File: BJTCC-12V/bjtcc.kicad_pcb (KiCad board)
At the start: 2 copper layers, 9 parts, among them J1 Screw_Terminal_1x04, P1 CONN_02X01, Q1 ASZ15, Q2 ASZ15

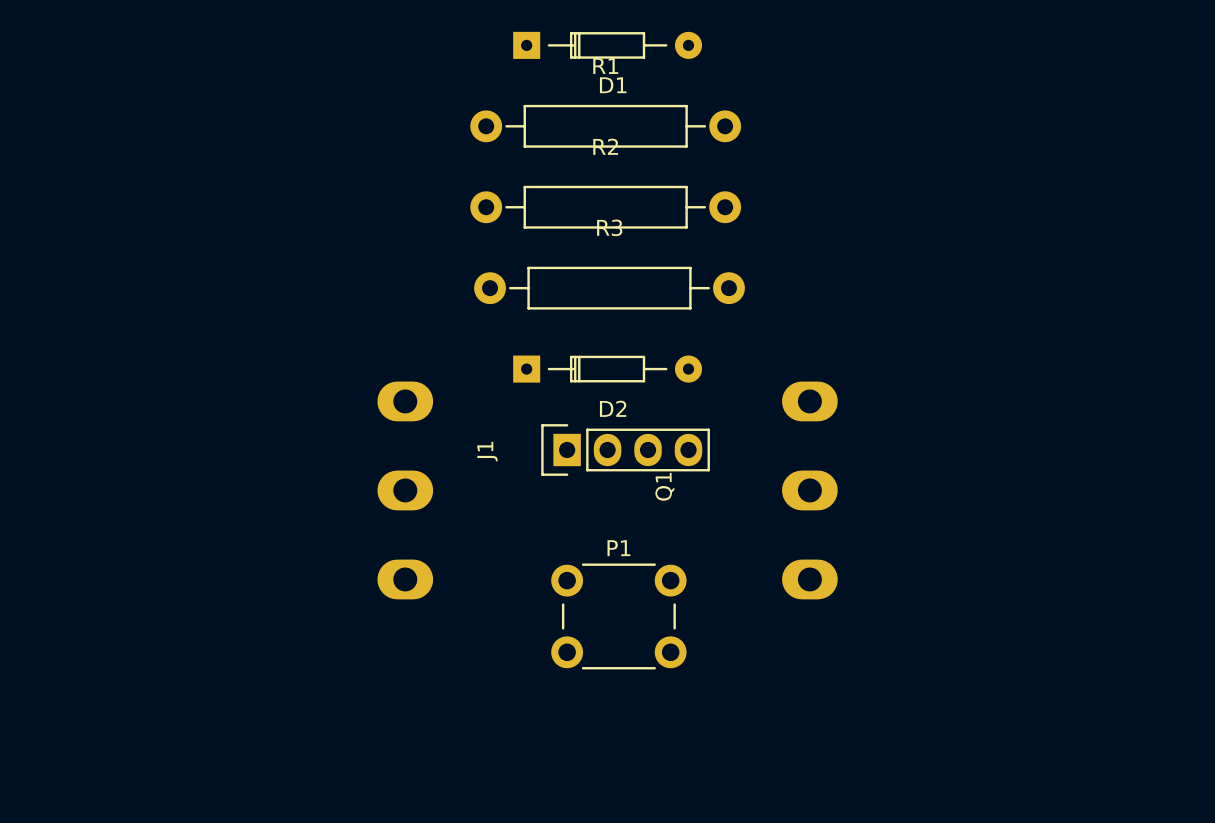
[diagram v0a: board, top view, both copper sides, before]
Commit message: rough placing footprints on PCB
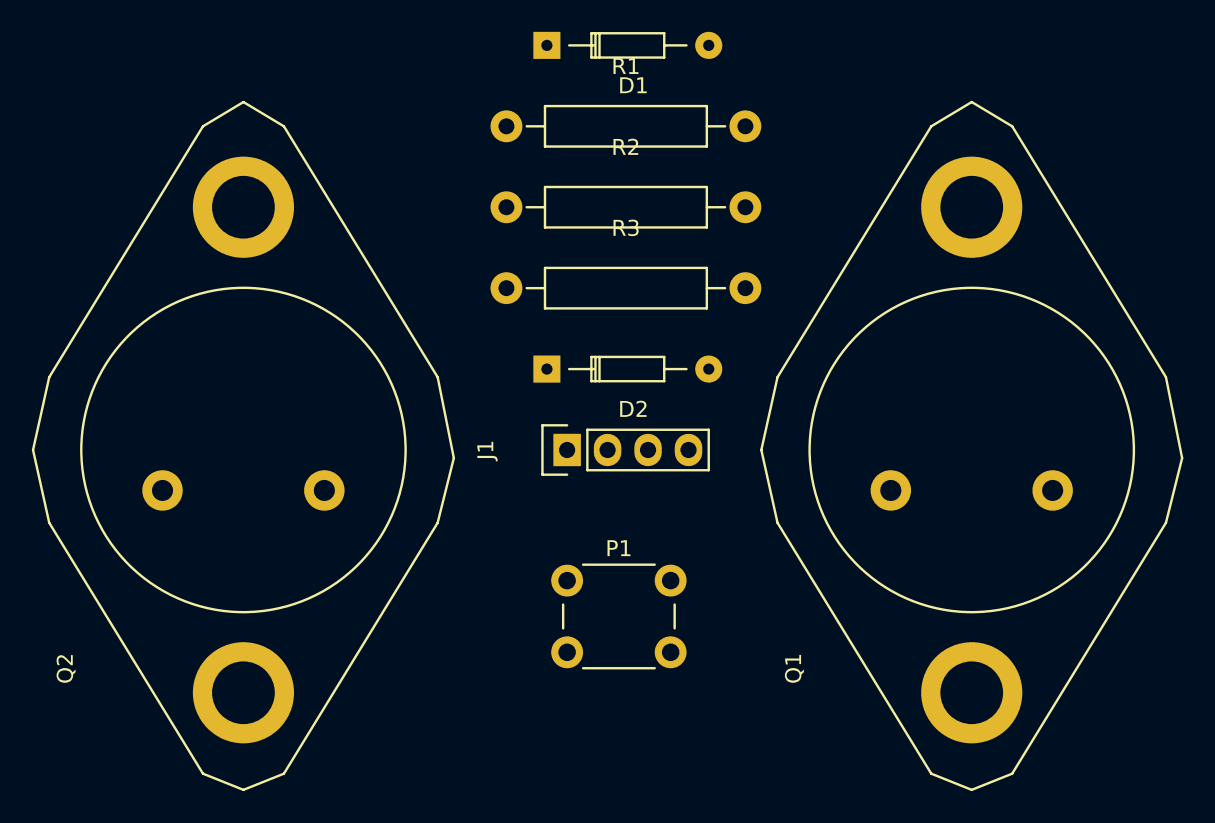
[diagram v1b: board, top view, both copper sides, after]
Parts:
- Q1: footprint TO_SOT_Packages_THT:TO-247_PadsOnly_Neutral123 -> TO_SOT_Packages_THT:TO3
- Q2: footprint TO_SOT_Packages_THT:TO-247_PadsOnly_Neutral123 -> TO_SOT_Packages_THT:TO3; moved to F.Cu
- moved Q2 15.2 mm to (154.9, 121.9)
- moved Q1 5.08 mm to (200.7, 121.9)
- moved D1 1.27 mm to (179.1, 94.0)
- moved D2 1.27 mm to (179.1, 114.3)
- moved R1 1.27 mm to (176.5, 99.1)
- moved R2 1.27 mm to (176.5, 104.1)
- moved R3 1.03 mm to (176.5, 109.2)
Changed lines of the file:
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@@
 (kicad_pcb (version 4) (host pcbnew 4.0.5+dfsg1-4)
   (general
-    (links 14)
-    (no_connects 11)
-    (area 0 0 0 0)
+    (links 16)
+    (no_connects 16)
+    (area 146.536999 89.449 219.223001 140.991001)
     (thickness 1.6)
     (drawings 0)
@@
   )
   (module Diodes_ThroughHole:Diode_DO-35_SOD27_Horizontal_RM10 (layer F.Cu)
-    (at 177.79948 93.98254)
+    (at 179.06948 93.98254)
     (descr "Diode, DO-35,  SOD27, Horizontal, RM 10mm")
     (tags "Diode, DO-35, SOD27, Horizontal, RM 10mm, 1N4148,")
@@
   )
   (module Diodes_ThroughHole:Diode_DO-35_SOD27_Horizontal_RM10 (layer F.Cu)
-    (at 177.79948 114.30254)
+    (at 179.06948 114.30254)
     (descr "Diode, DO-35,  SOD27, Horizontal, RM 10mm")
     (tags "Diode, DO-35, SOD27, Horizontal, RM 10mm, 1N4148,")
@@
     )
   )
-  (module TO_SOT_Packages_THT:TO-247_PadsOnly_Neutral123 (layer F.Cu)
-    (at 195.58 121.92 90)
-    (descr "TO-247, Neutral, Pads Only,")
-    (tags "TO-247, Neutral, Pads Only,")
-    (fp_text reference Q1 (at 0.254 -9.144 90) (layer F.SilkS)
-      (effects (font (size 1 1) (thickness 0.15)))
-    )
-    (fp_text value ASZ15 (at -1.016 8.128 90) (layer F.Fab)
-      (effects (font (size 1 1) (thickness 0.15)))
-    )
-    (pad 2 thru_hole oval (at 0 0 180) (size 3.50012 2.49936) (drill 1.50114) (layers *.Cu *.Mask)
-      (net 9 GND))
-    (pad 1 thru_hole oval (at -5.588 0 180) (size 3.50012 2.49936) (drill 1.50114) (layers *.Cu *.Mask)
-      (net 1 "Net-(D1-Pad2)"))
-    (pad 3 thru_hole oval (at 5.588 0 180) (size 3.50012 2.49936) (drill 1.50114) (layers *.Cu *.Mask)
-      (net 7 "Net-(J1-Pad3)"))
-  )
-  (module TO_SOT_Packages_THT:TO-247_PadsOnly_Neutral123 (layer B.Cu)
-    (at 170.18 121.92 90)
-    (descr "TO-247, Neutral, Pads Only,")
-    (tags "TO-247, Neutral, Pads Only,")
-    (fp_text reference Q2 (at 0.254 9.144 90) (layer B.SilkS)
-      (effects (font (size 1 1) (thickness 0.15)) (justify mirror))
-    )
-    (fp_text value ASZ15 (at -1.016 -8.128 90) (layer B.Fab)
-      (effects (font (size 1 1) (thickness 0.15)) (justify mirror))
-    )
-    (pad 2 thru_hole oval (at 0 0) (size 3.50012 2.49936) (drill 1.50114) (layers *.Cu *.Mask)
-      (net 9 GND))
-    (pad 1 thru_hole oval (at -5.588 0) (size 3.50012 2.49936) (drill 1.50114) (layers *.Cu *.Mask)
-      (net 3 "Net-(D2-Pad2)"))
-    (pad 3 thru_hole oval (at 5.588 0) (size 3.50012 2.49936) (drill 1.50114) (layers *.Cu *.Mask)
-      (net 6 "Net-(J1-Pad2)"))
-  )
   (module Resistors_ThroughHole:Resistor_Horizontal_RM15mm (layer F.Cu)
-    (at 175.26 99.06)
+    (at 176.53 99.06)
     (descr "Resistor, Axial, RM 15mm,")
     (tags "Resistor Axial RM 15mm")
@@
   )
   (module Resistors_ThroughHole:Resistor_Horizontal_RM15mm (layer F.Cu)
-    (at 175.26 104.14)
+    (at 176.53 104.14)
     (descr "Resistor, Axial, RM 15mm,")
     (tags "Resistor Axial RM 15mm")
@@
   )
   (module Resistors_ThroughHole:Resistor_Horizontal_RM15mm (layer F.Cu)
-    (at 175.5 109.22)
+    (at 176.53 109.22)
     (descr "Resistor, Axial, RM 15mm,")
     (tags "Resistor Axial RM 15mm")
@@
       (rotate (xyz 0 0 0))
     )
+  )
+  (module TO_SOT_Packages_THT:TO3 (layer F.Cu)
+    (at 200.66 121.92 90)
+    (descr "Transistor TO3")
+    (tags "TR TO3")
+    (fp_text reference Q1 (at -11.176 -6.096 90) (layer F.SilkS)
+      (effects (font (size 1 1) (thickness 0.15)))
+    )
+    (fp_text value ASZ15 (at -11.811 -4.064 90) (layer F.Fab)
+      (effects (font (size 1 1) (thickness 0.15)))
+    )
+    (fp_line (start -17.78 2.54) (end -18.796 5.08) (layer F.SilkS) (width 0.15))
+    (fp_line (start -18.796 5.08) (end -17.78 7.62) (layer F.SilkS) (width 0.15))
+    (fp_line (start 22.86 2.54) (end 24.384 5.08) (layer F.SilkS) (width 0.15))
+    (fp_line (start 24.384 5.08) (end 22.86 7.62) (layer F.SilkS) (width 0.15))
+    (fp_line (start -2.032 -7.112) (end 2.54 -8.128) (layer F.SilkS) (width 0.15))
+    (fp_line (start 2.54 -8.128) (end 7.112 -7.112) (layer F.SilkS) (width 0.15))
+    (fp_line (start -2.032 -7.112) (end -17.78 2.54) (layer F.SilkS) (width 0.15))
+    (fp_line (start 7.112 -7.112) (end 22.86 2.54) (layer F.SilkS) (width 0.15))
+    (fp_line (start 7.112 17.272) (end 22.86 7.62) (layer F.SilkS) (width 0.15))
+    (fp_line (start -2.032 17.272) (end -17.78 7.62) (layer F.SilkS) (width 0.15))
+    (fp_line (start 7.112 17.272) (end 2.032 18.288) (layer F.SilkS) (width 0.15))
+    (fp_line (start 2.032 18.288) (end -2.032 17.272) (layer F.SilkS) (width 0.15))
+    (fp_circle (center 2.54 5.08) (end 12.7 5.715) (layer F.SilkS) (width 0.15))
+    (pad 3 thru_hole circle (at -12.7 5.08 90) (size 6.35 6.35) (drill 3.937) (layers *.Cu *.Mask)
+      (net 7 "Net-(J1-Pad3)"))
+    (pad 3 thru_hole circle (at 17.78 5.08 90) (size 6.35 6.35) (drill 3.937) (layers *.Cu *.Mask)
+      (net 7 "Net-(J1-Pad3)"))
+    (pad 1 thru_hole circle (at 0 0 90) (size 2.54 2.54) (drill 1.3208) (layers *.Cu *.Mask)
+      (net 1 "Net-(D1-Pad2)"))
+    (pad 2 thru_hole circle (at 0 10.16 90) (size 2.54 2.54) (drill 1.3208) (layers *.Cu *.Mask)
+      (net 9 GND))
+    (model TO_SOT_Packages_THT.3dshapes/TO3.wrl
+      (at (xyz 0.1 -0.2 0))
+      (scale (xyz 1 1 1))
+      (rotate (xyz 0 0 0))
+    )
+  )
+  (module TO_SOT_Packages_THT:TO3 (layer F.Cu)
+    (at 154.94 121.92 90)
+    (descr "Transistor TO3")
+    (tags "TR TO3")
+    (fp_text reference Q2 (at -11.176 -6.096 90) (layer F.SilkS)
+      (effects (font (size 1 1) (thickness 0.15)))
+    )
+    (fp_text value ASZ15 (at -11.811 -4.064 90) (layer F.Fab)
+      (effects (font (size 1 1) (thickness 0.15)))
+    )
+    (fp_line (start -17.78 2.54) (end -18.796 5.08) (layer F.SilkS) (width 0.15))
+    (fp_line (start -18.796 5.08) (end -17.78 7.62) (layer F.SilkS) (width 0.15))
+    (fp_line (start 22.86 2.54) (end 24.384 5.08) (layer F.SilkS) (width 0.15))
+    (fp_line (start 24.384 5.08) (end 22.86 7.62) (layer F.SilkS) (width 0.15))
+    (fp_line (start -2.032 -7.112) (end 2.54 -8.128) (layer F.SilkS) (width 0.15))
+    (fp_line (start 2.54 -8.128) (end 7.112 -7.112) (layer F.SilkS) (width 0.15))
+    (fp_line (start -2.032 -7.112) (end -17.78 2.54) (layer F.SilkS) (width 0.15))
+    (fp_line (start 7.112 -7.112) (end 22.86 2.54) (layer F.SilkS) (width 0.15))
+    (fp_line (start 7.112 17.272) (end 22.86 7.62) (layer F.SilkS) (width 0.15))
+    (fp_line (start -2.032 17.272) (end -17.78 7.62) (layer F.SilkS) (width 0.15))
+    (fp_line (start 7.112 17.272) (end 2.032 18.288) (layer F.SilkS) (width 0.15))
+    (fp_line (start 2.032 18.288) (end -2.032 17.272) (layer F.SilkS) (width 0.15))
+    (fp_circle (center 2.54 5.08) (end 12.7 5.715) (layer F.SilkS) (width 0.15))
+    (pad 3 thru_hole circle (at -12.7 5.08 90) (size 6.35 6.35) (drill 3.937) (layers *.Cu *.Mask)
+      (net 6 "Net-(J1-Pad2)"))
+    (pad 3 thru_hole circle (at 17.78 5.08 90) (size 6.35 6.35) (drill 3.937) (layers *.Cu *.Mask)
+      (net 6 "Net-(J1-Pad2)"))
+    (pad 1 thru_hole circle (at 0 0 90) (size 2.54 2.54) (drill 1.3208) (layers *.Cu *.Mask)
+      (net 3 "Net-(D2-Pad2)"))
+    (pad 2 thru_hole circle (at 0 10.16 90) (size 2.54 2.54) (drill 1.3208) (layers *.Cu *.Mask)
+      (net 9 GND))
+    (model TO_SOT_Packages_THT.3dshapes/TO3.wrl
+      (at (xyz 0.1 -0.2 0))
+      (scale (xyz 1 1 1))
+      (rotate (xyz 0 0 0))
+    )
